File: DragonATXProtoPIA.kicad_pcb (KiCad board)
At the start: 2 copper layers, 168.7 x 97.2 mm, 80 parts, among them IC1 MC6821, IC10 MT8816, IC11 74LS138, IC12 W65C51, IC13 MAX232, IC14 M48Tx2, IC15 74LS21, IC2 MC6821, IC3 74LS138, IC4 4050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

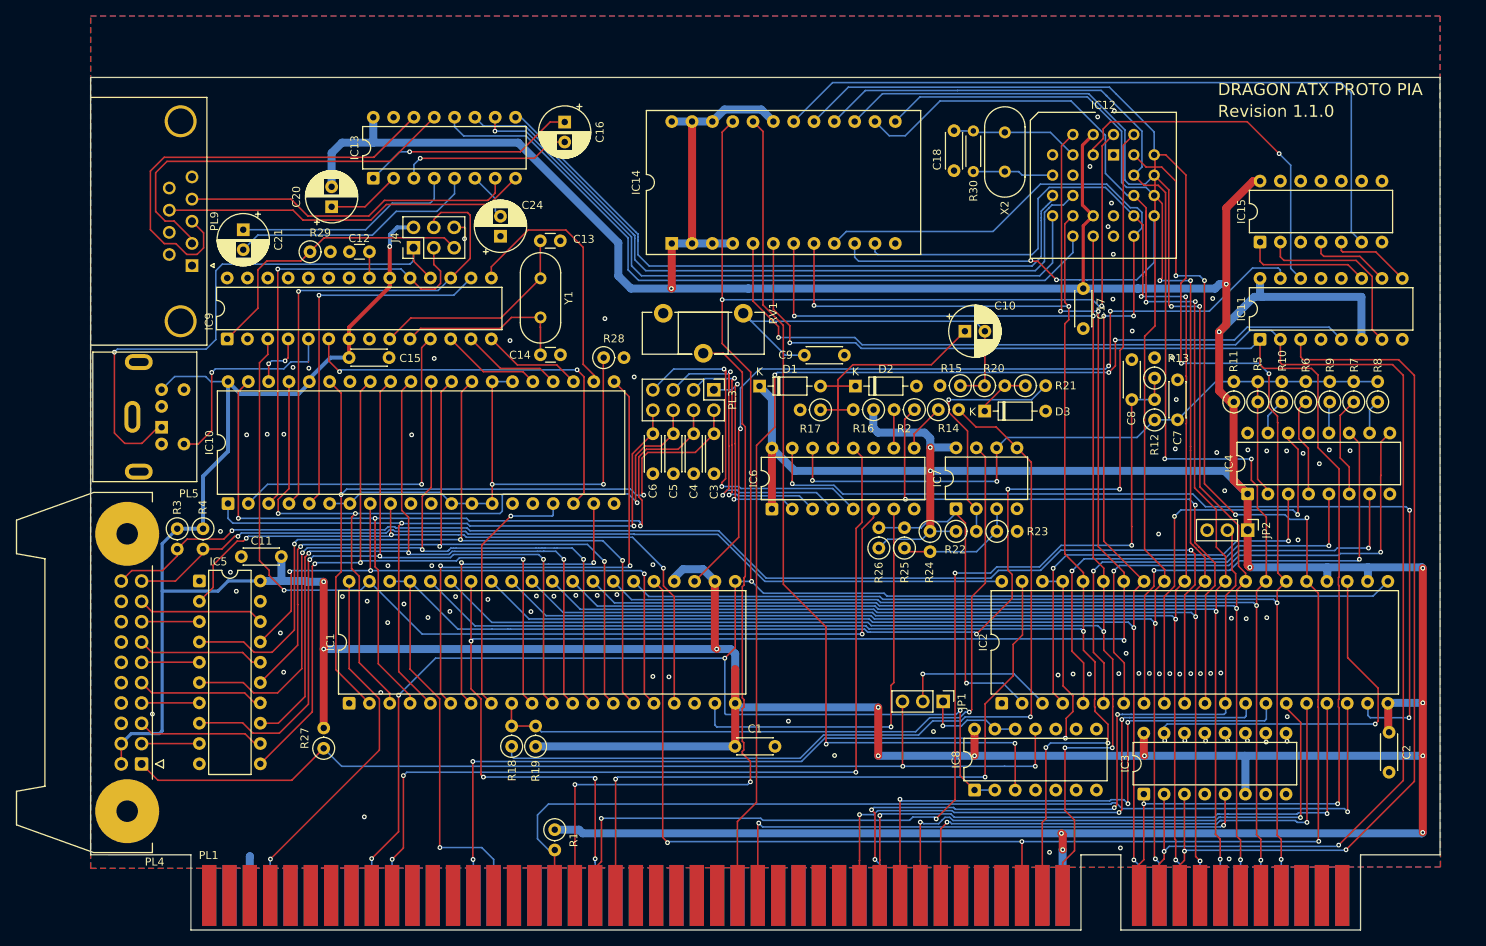
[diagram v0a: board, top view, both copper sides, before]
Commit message: remove uart and rtc
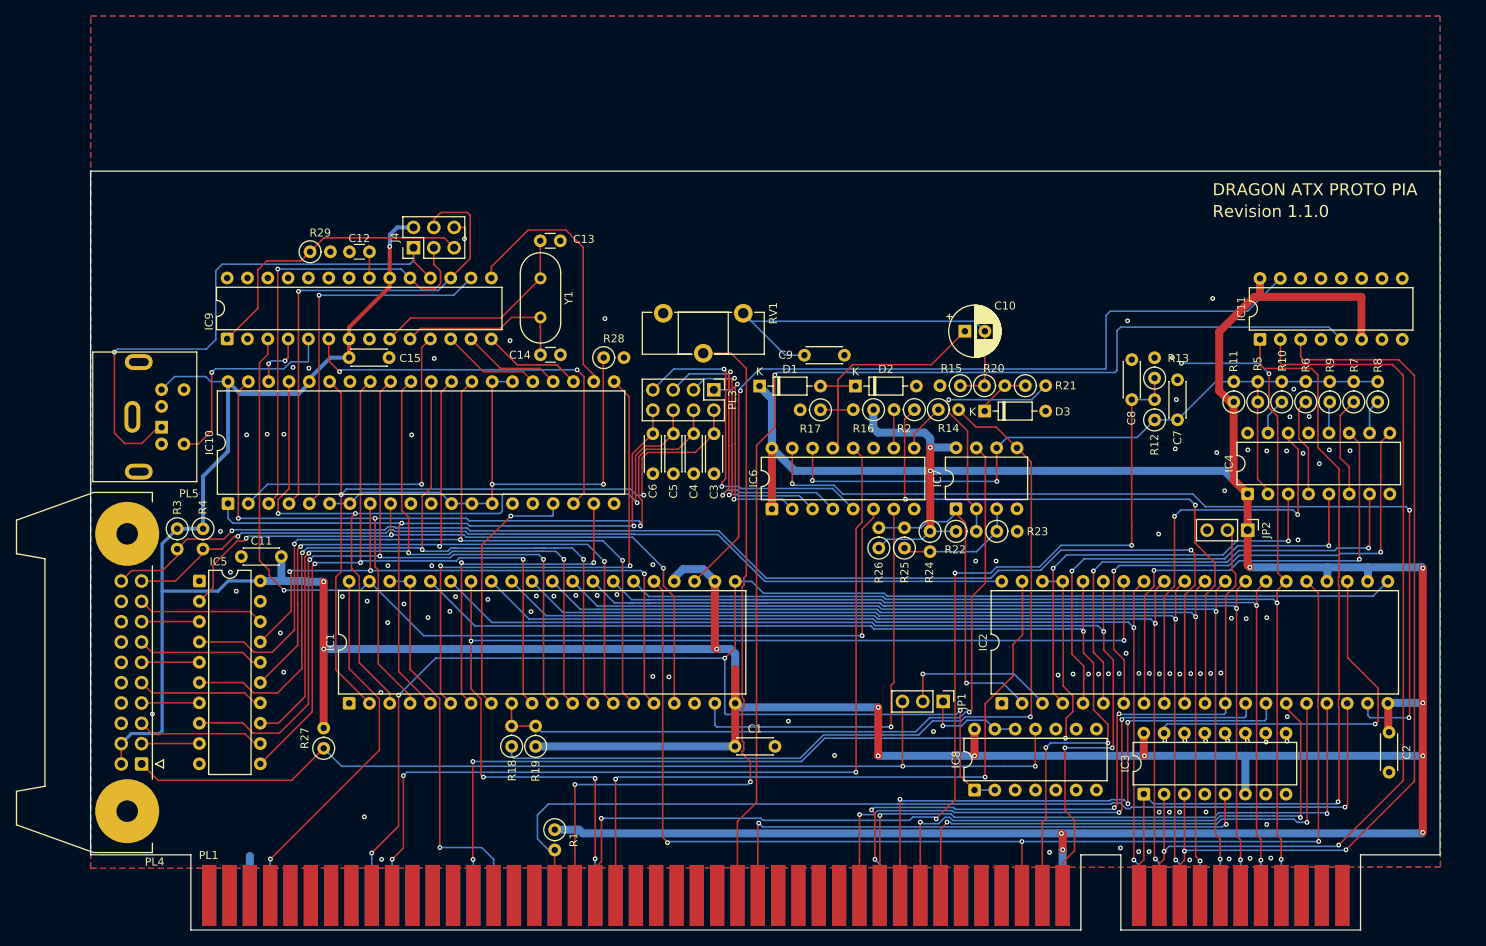
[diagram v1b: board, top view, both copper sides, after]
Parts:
- removed C16, C20, C21, C24: 10u, Capacitor_THT:CP_Radial_D6.3mm_P2.50mm
- removed C17: 100n, Capacitor_THT:C_Disc_D4.3mm_W1.9mm_P5.00mm
- removed C18: 30pF, Capacitor_THT:C_Disc_D4.3mm_W1.9mm_P5.00mm
- removed IC12: W65C51, Package_LCC:PLCC-28_THT-Socket
- removed IC13: MAX232, Package_DIP:DIP-16_W7.62mm
- removed IC14: M48Tx2, Package_DIP:DIP-24_18.0mmx34.29mm_W15.24mm
- removed IC15: 74LS21, Package_DIP:DIP-14_W7.62mm
- removed PL9: rs232 serial port, Connector_Dsub:DSUB-9_Socket_Horizontal_P2.77x2.84mm_EdgePinOffset9.90mm_Housed_MountingHolesOffset11.32mm
- removed R30: 1M, Resistor_THT:R_Axial_DIN0204_L3.6mm_D1.6mm_P5.08mm_Horizontal
- removed X2: 1.8432MHz, Crystal:Crystal_HC18-U_Vertical
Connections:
- IC8 pad 1: /R/W -> GND
- IC8 pad 2: /R/W -> GND
- IC8 pad 3: Net-(IC14-~{G}) -> unconnected-(IC8-Pad3)
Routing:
- net +5V: track 927.8 -> 713.0 mm, vias 20 -> 17
- net /IRQ: track 201.9 -> 49.2 mm, vias 4 -> 1
- net /R/W: track 341.6 -> 212.2 mm, vias 7 -> 4
- net /D6: track 235.0 -> 121.7 mm, vias 4 -> 2
- net Net-(IC14-~{G}): track 111.2 -> 0.00 mm, vias 2 -> 0
- net /D4: track 229.4 -> 122.1 mm, vias 4 -> 2
- net /D5: track 227.2 -> 121.8 mm, vias 4 -> 2
- net /D1: track 225.1 -> 122.7 mm, vias 4 -> 2
- net /D3: track 218.1 -> 122.2 mm, vias 4 -> 2
- net /D0: track 218.2 -> 122.9 mm, vias 4 -> 2
- net /D2: track 216.6 -> 122.4 mm, vias 4 -> 2
- net /RxD: track 92.3 -> 0.00 mm
- net /TxD: track 91.9 -> 0.00 mm
- net /P0U: track 91.4 -> 0.00 mm
- net /A1: track 221.2 -> 131.1 mm, vias 5 -> 3
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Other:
- board size 168.7 x 97.2 mm -> 168.7 x 85.5 mm

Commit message: prepare for fabrication
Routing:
- net /R/W: track 212.2 -> 162.4 mm, vias 4 -> 3
- net +5V: track 713.0 -> 708.8 mm, vias 17 -> 16
- net Net-(IC4-Pad2): track 15.0 -> 12.1 mm
- net GND: track 7.35 -> 9.89 mm, vias 102 -> 103
- net X2: track 41.2 -> 39.4 mm
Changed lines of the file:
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@@
 	)
 	(footprint "Library:Card_Edge"
+		(locked yes)
 		(layer "F.Cu")
 		(at 116.9284 127.0687)
@@
 		(sheetname "/")
 		(sheetfile "DragonATXProtoPIA.kicad_sch")
-		(attr smd)
+		(attr smd exclude_from_bom)
 		(fp_line
 			(start 85.5142 15.242937)
@@
 	)
 	(segment
+		(start 108.8948 105.6082)
+		(end 108.8644 105.6386)
+		(width 1)
+		(layer "F.Cu")
+		(net 1)
+	)
+	(segment
 		(start 149.8346 118.5545)
 		(end 149.8346 116.6749)
@@
 	)
 	(segment
+		(start 108.8948 100.2538)
+		(end 108.8948 105.6082)
+		(width 1)
+		(layer "F.Cu")
+		(net 1)
+	)
+	(segment
 		(start 169.3926 61.2068)
 		(end 171.196 63.0102)
@@
 	)
 	(segment
-		(start 159.9692 106.7435)
-		(end 159.9692 103.9876)
-		(width 1)
-		(layer "F.Cu")
-		(net 1)
-	)
-	(segment
 		(start 106.5784 93.472)
 		(end 106.3498 93.2434)
@@
 	)
 	(segment
-		(start 108.8948 95.9739)
-		(end 108.8948 105.6082)
-		(width 1)
-		(layer "F.Cu")
-		(net 1)
-	)
-	(segment
 		(start 138.811 106.8197)
 		(end 138.811 103.4796)
@@
 	)
 	(segment
-		(start 160.0454 106.8197)
-		(end 159.9692 106.7435)
-		(width 1)
-		(layer "F.Cu")
-		(net 1)
-	)
-	(segment
-		(start 108.8948 105.6082)
-		(end 108.8644 105.6386)
-		(width 1)
-		(layer "F.Cu")
-		(net 1)
-	)
-	(segment
 		(start 133.2774 68.2752)
 		(end 133.2774 78.7328)
@@
 	)
 	(via
-		(at 160.0454 106.8197)
-		(size 0.6)
-		(drill 0.3)
-		(layers "F.Cu" "B.Cu")
-		(net 1)
-	)
-	(via
 		(at 133.2992 71.2039)
 		(size 0.6)
@@
 	)
 	(segment
+		(start 159.9692 106.7435)
+		(end 159.9692 103.9876)
+		(width 1)
+		(layer "B.Cu")
+		(net 1)
+	)
+	(segment
 		(start 66.6496 40.767)
 		(end 68.6816 40.767)
@@
 	)
 	(segment
+		(start 160.0454 106.8197)
+		(end 159.9692 106.7435)
+		(width 1)
+		(layer "B.Cu")
+		(net 1)
+	)
+	(segment
 		(start 113.4854 62.2028)
 		(end 111.934 60.6514)
@@
 	)
 	(via
-		(at 175.26 105.0925)
+		(at 183.1594 68.58)
 		(size 0.6)
 		(drill 0.3)
@@
 	)
 	(via
-		(at 167.6908 104.9528)
+		(at 177.927 105.664)
 		(size 0.6)
 		(drill 0.3)
@@
 	)
 	(via
-		(at 183.1594 68.58)
+		(at 172.6184 105.664)
 		(size 0.6)
 		(drill 0.3)
@@
 	)
 	(via
-		(at 52.0446 91.4654)
+		(at 162.5854 105.664)
 		(size 0.6)
 		(drill 0.3)
@@
 	)
 	(via
-		(at 157.9372 52.451)
+		(at 52.0446 91.4654)
 		(size 0.6)
 		(drill 0.3)
@@
 	)
 	(via
-		(at 161.8234 79.0956)
+		(at 157.9372 52.451)
 		(size 0.6)
 		(drill 0.3)
@@
 	)
 	(via
-		(at 173.2534 119.634)
+		(at 161.8234 79.0956)
 		(size 0.6)
 		(drill 0.3)
@@
 	)
 	(via
-		(at 163.1696 113.8682)
+		(at 173.2534 119.634)
 		(size 0.6)
 		(drill 0.3)
@@
 	)
 	(via
-		(at 53.6194 58.2676)
+		(at 163.1696 113.8682)
 		(size 0.6)
 		(drill 0.3)
@@
 	)
 	(via
-		(at 100.6094 96.9518)
+		(at 53.6194 58.2676)
 		(size 0.6)
 		(drill 0.3)
@@
 	)
 	(via
-		(at 177.8762 104.9959)
+		(at 100.6094 96.9518)
 		(size 0.6)
 		(drill 0.3)
@@
 	)
 	(via
-		(at 165.1 104.9147)
-		(size 0.6)
-		(drill 0.3)
-		(layers "F.Cu" "B.Cu")
-		(free yes)
-		(net 2)
-	)
-	(via
 		(at 44.5516 78.7654)
 		(size 0.6)
@@
 	)
 	(via
-		(at 170.434 104.9147)
+		(at 62.8904 87.4903)
 		(size 0.6)
 		(drill 0.3)
@@
 	)
 	(via
-		(at 62.8904 87.4903)
+		(at 164.0288 62.2935)
 		(size 0.6)
 		(drill 0.3)
@@
 	)
 	(via
-		(at 164.0288 62.2935)
+		(at 167.64 105.6894)
 		(size 0.6)
 		(drill 0.3)
@@
 	)
 	(via
-		(at 162.5854 104.9147)
-		(size 0.6)
-		(drill 0.3)
-		(layers "F.Cu" "B.Cu")
-		(free yes)
-		(net 2)
-	)
-	(via
 		(at 159.3342 118.7958)
 		(size 0.6)
@@
 	)
 	(via
+		(at 165.0492 105.664)
+		(size 0.6)
+		(drill 0.3)
+		(layers "F.Cu" "B.Cu")
+		(free yes)
+		(net 2)
+	)
+	(via
 		(at 180.6448 64.4144)
 		(size 0.6)
@@
 	)
 	(via
+		(at 175.26 105.7148)
+		(size 0.6)
+		(drill 0.3)
+		(layers "F.Cu" "B.Cu")
+		(free yes)
+		(net 2)
+	)
+	(via
 		(at 62.5348 114.4524)
 		(size 0.6)
@@
 	)
 	(via
-		(at 172.9232 104.9147)
+		(at 92.6084 52.1716)
 		(size 0.6)
 		(drill 0.3)
@@
 	)
 	(via
-		(at 92.6084 52.1716)
+		(at 98.6028 96.901)
 		(size 0.6)
 		(drill 0.3)
@@
 	)
 	(via
-		(at 98.6028 96.901)
+		(at 170.1292 105.6132)
 		(size 0.6)
 		(drill 0.3)
@@
 	)
 	(via
+		(at 160.0454 108.9914)
+		(size 0.6)
+		(drill 0.3)
+		(layers "F.Cu" "B.Cu")
+		(free yes)
+		(net 2)
+	)
+	(via
 		(at 170.9166 89.6239)
 		(size 0.6)
@@
 	)
 	(segment
+		(start 138.811 111.0996)
+		(end 141.351 111.0996)
+		(width 0.2)
+		(layer "B.Cu")
+		(net 2)
+	)
+	(segment
 		(start 48.2214 119.3855)
 		(end 48.2346 119.3723)
@@
 	)
 	(segment
-		(start 137.0076 109.2962)
-		(end 138.811 111.0996)
-		(width 0.2)
-		(layer "F.Cu")
-		(net 20)
-	)
-	(segment
 		(start 63.4492 118.9736)
 		(end 66.8158 115.607)
@@
 	)
 	(segment
-		(start 137.024104 101.141367)
-		(end 137.0076 101.157871)
-		(width 0.2)
-		(layer "F.Cu")
-		(net 20)
-	)
-	(segment
-		(start 137.0076 101.157871)
-		(end 137.0076 109.2962)
-		(width 0.2)
-		(layer "F.Cu")
-		(net 20)
-	)
-	(segment
 		(start 66.8158 115.607)
 		(end 66.8158 99.2378)
@@
 		(net 20)
 	)
-	(via
-		(at 137.024104 101.141367)
-		(size 0.6)
-		(drill 0.3)
-		(layers "F.Cu" "B.Cu")
-		(net 20)
-	)
 	(segment
 		(start 66.8158 99.2378)
@@
 	)
 	(segment
-		(start 138.811 111.0996)
-		(end 141.351 111.0996)
-		(width 0.2)
-		(layer "B.Cu")
-		(net 20)
-	)
-	(segment
-		(start 107.5944 101.5238)
-		(end 107.5944 94.615)
-		(width 0.2)
-		(layer "B.Cu")
-		(net 20)
-	)
-	(segment
-		(start 107.7214 101.6508)
-		(end 107.5944 101.5238)
-		(width 0.2)
-		(layer "B.Cu")
-		(net 20)
-	)
-	(segment
 		(start 63.4492 118.9736)
 		(end 63.4492 119.6721)
@@
 	)
 	(segment
-		(start 136.514671 101.6508)
-		(end 107.7214 101.6508)
-		(width 0.2)
-		(layer "B.Cu")
-		(net 20)
-	)
-	(segment
 		(start 127.8636 86.8588)
 		(end 188.6296 86.8588)
@@
 	)
 	(segment
-		(start 137.024104 101.141367)
-		(end 136.514671 101.6508)
-		(width 0.2)
-		(layer "B.Cu")
-		(net 20)
-	)
-	(segment
 		(start 63.4492 119.6721)
 		(end 63.4614 119.6843)
@@
 	)
 	(segment
+		(start 174.1932 72.263)
+		(end 174.1932 62.611)
+		(width 0.2)
+		(layer "F.Cu")
+		(net 77)
+	)
+	(segment
 		(start 175.4886 73.5584)
 		(end 174.1932 72.263)
@@
 	)
 	(segment
-		(start 175.4886 74.0918)
-		(end 175.4886 73.5584)
+		(start 174.1932 62.611)
+		(end 174.2186 62.5856)
 		(width 0.2)
 		(layer "F.Cu")
@@
 	)
 	(segment
-		(start 174.1932 72.263)
-		(end 174.1932 59.6723)
+		(start 175.4886 74.0918)
+		(end 175.4886 73.5584)
 		(width 0.2)
 		(layer "F.Cu")
@@
 	)
 	(segment
-		(start 107.6928 59.064282)
-		(end 107.6918 59.063282)
-		(width 0.2)
-		(layer "F.Cu")
-		(net 92)
-	)
-	(segment
 		(start 107.6928 72.192539)
 		(end 107.6928 58.6735)
@@
 	)
 	(segment
-		(start 107.6918 59.063282)
-		(end 107.6918 58.6725)
-		(width 0.2)
-		(layer "F.Cu")
-		(net 92)
-	)
-	(segment
 		(start 107.6918 58.6725)
 		(end 107.4928 58.4735)
@@
 		(width 0.2)
 		(layer "F.Cu")
-		(net 93)
-	)
-	(segment
-		(start 108.0938 59.052162)
-		(end 108.0938 60.9151)
-		(width 0.2)
-		(layer "F.Cu")
